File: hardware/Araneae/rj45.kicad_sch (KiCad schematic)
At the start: 46 parts, among them J13 RJ45_JK0654219, J14 RJ45_JK0654219

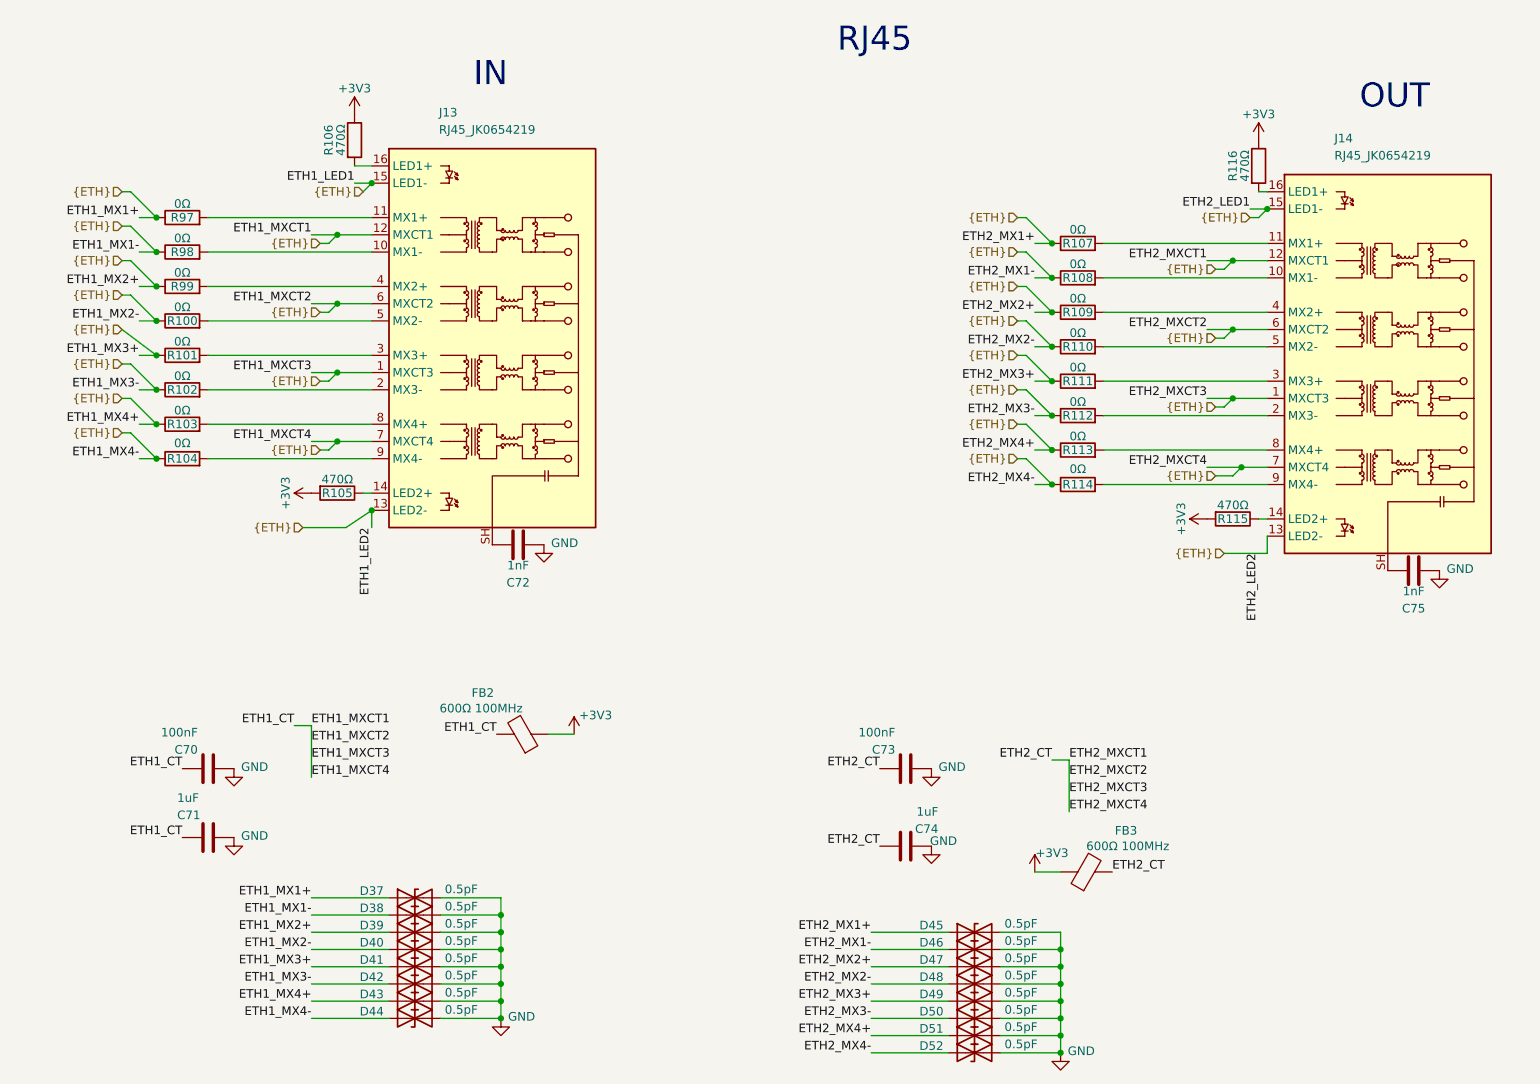
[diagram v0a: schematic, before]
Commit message: Add CI workflow for PCB checks and artifact generation
- Created a GitHub Actions workflow (`ci.yml`) to automate hardware checks including ERC, DRC, and plot generation for KiCad projects.
- Added a new footprint for the SON50P200X200X80-9N component in `SON50P200X200X80-9N.kicad_mod`.
- Introduced a new symbol for the TPS22965DSGR component in `TPS22965DSGR.kicad_sym`.
- Added a configuration file `kibot.yaml` for generating fabrication files and other outputs.
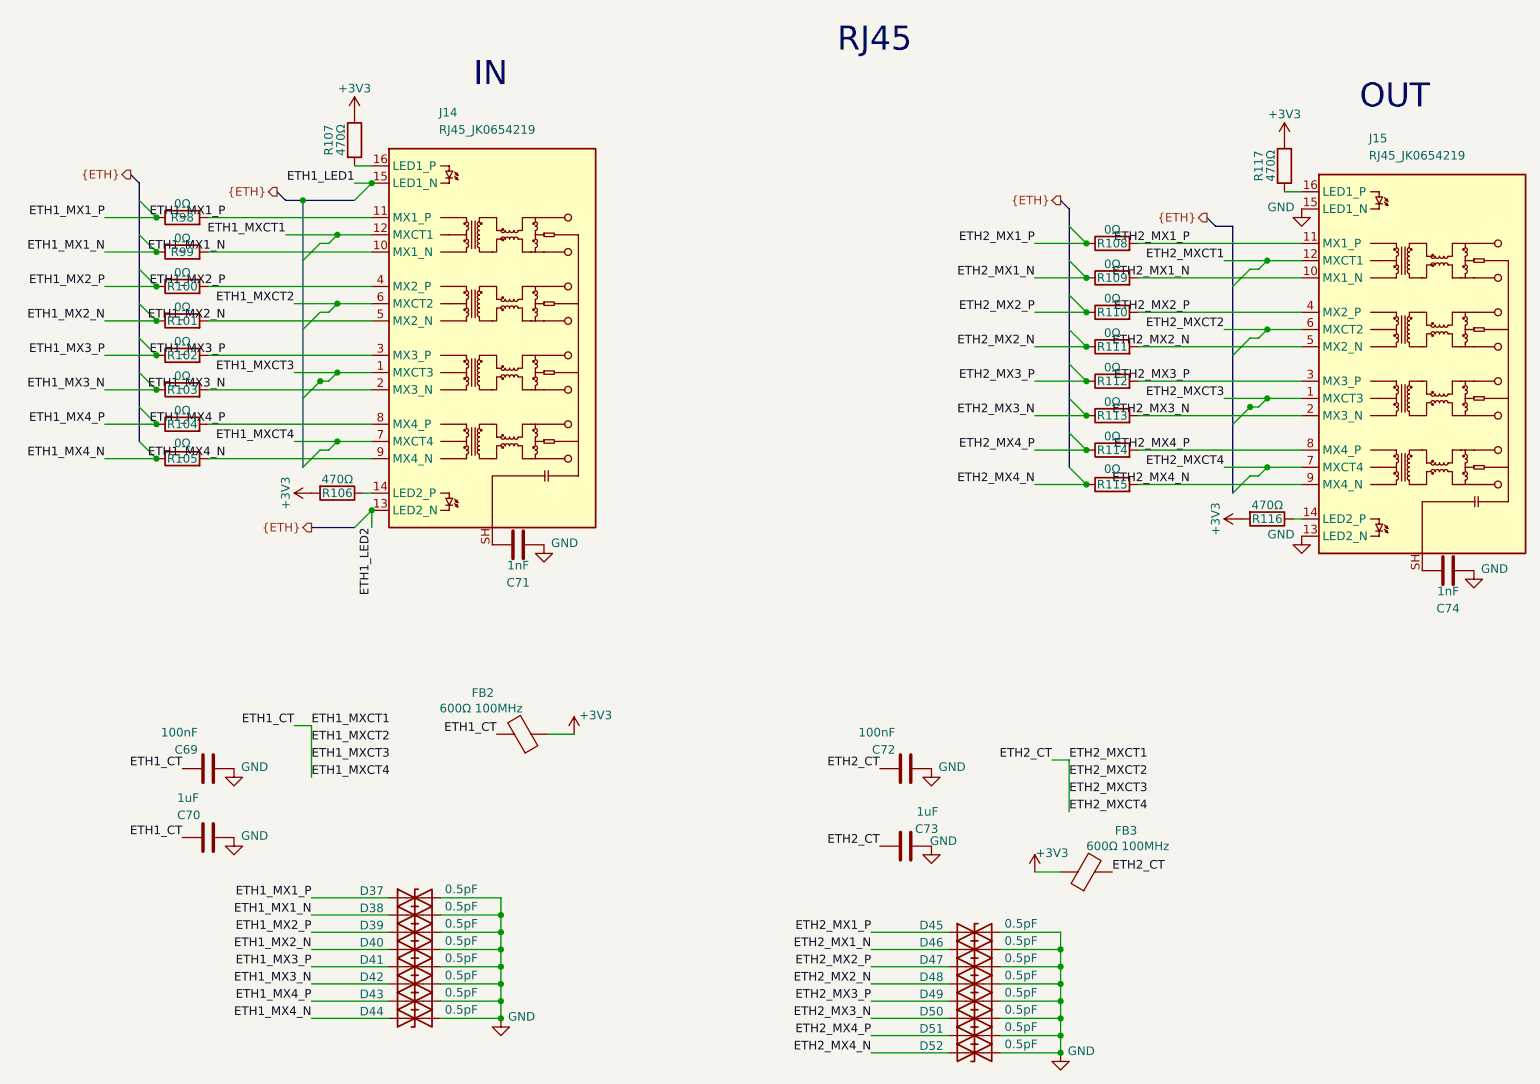
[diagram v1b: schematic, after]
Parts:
- removed C75: 1nF, symbol Device:C
- removed J14: RJ45_JK0654219, Connector_RJ:RJ45_Pulse_JK0654219NL_Horizontal, symbol Connector:RJ45_JK0654219
- removed R107: 0Ω, symbol Device:R
- added C74: 1nF, Capacitor_SMD:C_0603_1608Metric, symbol Device:C
- added J15: RJ45_JK0654219, Connector_RJ:RJ45_Pulse_JK0654219NL_Horizontal, symbol Connector:RJ45_JK0654219
- added R117: 470Ω, Resistor_SMD:R_0603_1608Metric, symbol Device:R
- C69: renamed from C70; footprint (none) -> Capacitor_SMD:C_0805_2012Metric
- C70: renamed from C71; footprint (none) -> Capacitor_SMD:C_0603_1608Metric
- C71: renamed from C72; footprint (none) -> Capacitor_SMD:C_0603_1608Metric
- C72: renamed from C73; footprint (none) -> Capacitor_SMD:C_0603_1608Metric
- C73: renamed from C74; footprint (none) -> Capacitor_SMD:C_0603_1608Metric
- D37, D38, D39, D40, D41, D42, D43, D44, D45, D46, D47, D48, D49, D50, D51, D52: footprint (none) -> Diode_SMD:D_SOD-523
- FB2, FB3: footprint (none) -> Inductor_SMD:L_0805_2012Metric
- R100: renamed from R99; footprint (none) -> Resistor_SMD:R_0603_1608Metric
- R101: renamed from R100; footprint (none) -> Resistor_SMD:R_0603_1608Metric
- R102: renamed from R101; footprint (none) -> Resistor_SMD:R_0603_1608Metric
- R103: renamed from R102; footprint (none) -> Resistor_SMD:R_0603_1608Metric
- R104: renamed from R103; footprint (none) -> Resistor_SMD:R_0603_1608Metric
- R105: renamed from R104; footprint (none) -> Resistor_SMD:R_0603_1608Metric
- R106: renamed from R105; footprint (none) -> Resistor_SMD:R_0603_1608Metric
- R107: renamed from R106; footprint (none) -> Resistor_SMD:R_0603_1608Metric
- R108, R109, R110, R111, R112, R113, R114, R116: footprint (none) -> Resistor_SMD:R_0603_1608Metric
- R115: value 470Ω -> 0Ω; footprint (none) -> Resistor_SMD:R_0603_1608Metric
- R98: renamed from R97; footprint (none) -> Resistor_SMD:R_0603_1608Metric
- R99: renamed from R98; footprint (none) -> Resistor_SMD:R_0603_1608Metric
- renumbered J13 to J14
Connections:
- net +3V3: now also R116.2, R117.1; no longer R115.2, R116.1
- net GND: now also C74.2, J15.13 (LED2_N), J15.15 (LED1_N)
- net {ETH}: no longer C69.1, C70.2, C72.1, C73.1, D37.1 (A1), D38.1 (A1), D39.1 (A1), D40.1 (A1), D41.1 (A1), D42.1 (A1), D43.1 (A1), D44.1 (A1), D45.1 (A1), D46.1 (A1), D47.1 (A1), D48.1 (A1), D49.1 (A1), D50.1 (A1), D51.1 (A1), D52.1 (A1), FB2.2, FB3.2, J14.1 (MXCT3), J14.12 (MXCT1), J14.13 (LED2-), J14.15 (LED1-), J14.6 (MXCT2), J14.7 (MXCT4), R100.1, R101.1, R102.1, R103.1, R104.1, R105.1, R108.1, R109.1, R110.1, R111.1, R112.1, R113.1, R114.1, R98.1, R99.1
- net ETH2_MX2_P: now reaches R110.2
- net ETH2_MX2_P: now also D47.1 (A1), R110.1, J15.4 (MX2_P)
- net ETH2_MX1_N: now reaches R109.2
- net ETH2_MX1_N: now also D46.1 (A1), R109.1, J15.10 (MX1_N)
- net ETH2_MX4_N: now reaches R115.1
- net ETH2_MX4_N: now also D52.1 (A1), R115.2, J15.9 (MX4_N)
- net ETH1_MX1_P: now reaches J14.11 (MX1_P), R98.2
- net ETH1_MX1_P: now also D37.1 (A1), R98.1
- net ETH1_MX2_N: now reaches J14.5 (MX2_N), R101.2
- net ETH1_MX2_N: now also D40.1 (A1), R101.1
- net ETH2_MX3_P: now reaches R112.2
- net ETH2_MX3_P: now also D49.1 (A1), R112.1, J15.3 (MX3_P)
- net ETH1_MX1_N: now reaches J14.10 (MX1_N), R99.2
- net ETH1_MX1_N: now also D38.1 (A1), R99.1
- net ETH1_MX3_N: now reaches J14.2 (MX3_N), R103.2
- net ETH1_MX3_N: now also D42.1 (A1), R103.1
- net ETH1_MX3_P: now reaches J14.3 (MX3_P), R102.2
- net ETH1_MX3_P: now also D41.1 (A1), R102.1
- net ETH1_MX2_P: now reaches J14.4 (MX2_P), R100.2
- net ETH1_MX2_P: now also D39.1 (A1), R100.1
- net ETH1_MX4_P: now reaches J14.8 (MX4_P), R104.2
- net ETH1_MX4_P: now also D43.1 (A1), R104.1
- net ETH1_MX4_N: now reaches J14.9 (MX4_N), R105.2
- net ETH1_MX4_N: now also D44.1 (A1), R105.1
- net ETH2_MX2_N: now reaches R111.2
- net ETH2_MX2_N: now also D48.1 (A1), R111.1, J15.5 (MX2_N)
- net ETH2_MX3_N: now reaches R113.2
- net ETH2_MX3_N: now also D50.1 (A1), R113.1, J15.2 (MX3_N)
- net ETH2_MX1_P: now reaches R108.2
- net ETH2_MX1_P: now also D45.1 (A1), R108.1, J15.11 (MX1_P)
- net ETH2_MX4_P: now reaches R114.2
- net ETH2_MX4_P: now also D51.1 (A1), R114.1, J15.8 (MX4_P)
- new net: J15.14 (LED2_P), R116.1
- new net: J15.16 (LED1_P), R117.2
- new net: C74.1, J15.SH
- new net ETH1_CT: C69.1, C70.2, FB2.2, J14.1 (MXCT3), J14.12 (MXCT1), J14.6 (MXCT2), J14.7 (MXCT4)
- new net ETH1_LED1: J14.15 (LED1_N)
- new net ETH1_LED2: J14.13 (LED2_N)
- new net ETH2_CT: C72.1, C73.1, FB3.2, J15.1 (MXCT3), J15.12 (MXCT1), J15.6 (MXCT2), J15.7 (MXCT4)
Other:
- company: (none) -> Matheus Henrique(Aka: TheusHen)
- title: (none) -> Araneae
